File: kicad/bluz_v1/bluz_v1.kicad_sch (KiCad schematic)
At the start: 71 parts, among them J1 USB_B_Micro, J10 Conn, J11 Conn, J12 BTAnt, J2 Conn, J3 Conn, J4 Conn, J5 Conn, J6 Conn, J7 Conn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

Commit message: изменено:      kicad/bluz_v1/bluz_v1.kicad_pcb 	изменено:      kicad/bluz_v1/bluz_v1.kicad_sch
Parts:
- L2: value 47uH -> 47uH LQH31CN470K03L
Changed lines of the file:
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@@
       (effects (font (size 1.27 1.27)) hide)
     )
-    (property "Value" "47uH" (id 1) (at 164.465 28.1741 90))
+    (property "Value" "47uH LQH31CN470K03L" (id 1) (at 159.385 27.305 90))
     (property "Footprint" "Inductor_SMD:L_1206_3216Metric" (id 2) (at 164.465 29.845 0)
       (effects (font (size 1.27 1.27)) hide)
@@
       (effects (font (size 1.27 1.27)) hide)
     )
-    (property "Value" "+BATT" (id 1) (at 151.765 27.94 90)
+    (property "Value" "+BATT" (id 1) (at 147.955 29.845 90)
       (effects (font (size 1.27 1.27)) (justify right))
     )
@@
     )
     (path "/77373934-a013-4003-ae17-82edd2463c24"
-      (reference "L2") (unit 1) (value "47uH") (footprint "Inductor_SMD:L_1206_3216Metric")
+      (reference "L2") (unit 1) (value "47uH LQH31CN470K03L") (footprint "Inductor_SMD:L_1206_3216Metric")
     )
     (path "/fd18f754-2e4f-4eb7-a1de-4025462c7606"

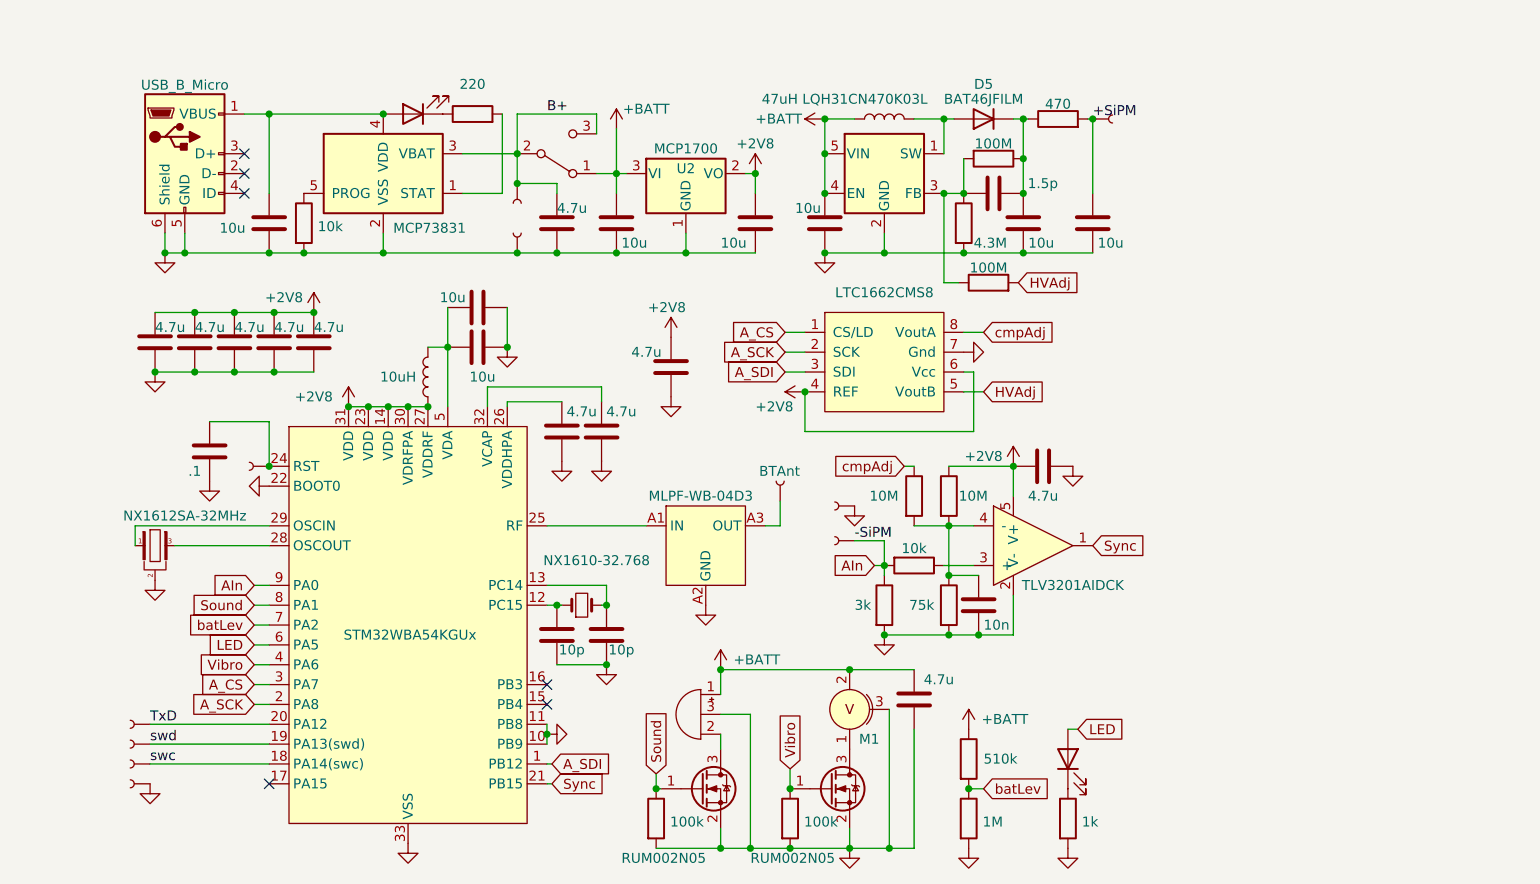
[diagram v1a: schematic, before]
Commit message: изменено:      kicad/bluz_v1/bluz_v1.kicad_sch 	изменено:      stm32cubeide/BluZ_v1/.mxproject 	изменено:      stm32cubeide/BluZ_v1/BluZ_v1.ioc 	изменено:      stm32cubeide/BluZ_v1/Core/Inc/app_conf.h 	изменено:      stm32cubeide/BluZ_v1/Core/Src/main.c 	изменено:      stm32cubeide/BluZ_v1/Release/BluZ_v1.hex 	изменено:      stm32cubeide/BluZ_v1/Release/BluZ_v1.list 	изменено:      stm32cubeide/BluZ_v1/Release/BluZ_v1.map 	изменено:      stm32cubeide/BluZ_v1/Release/makefile
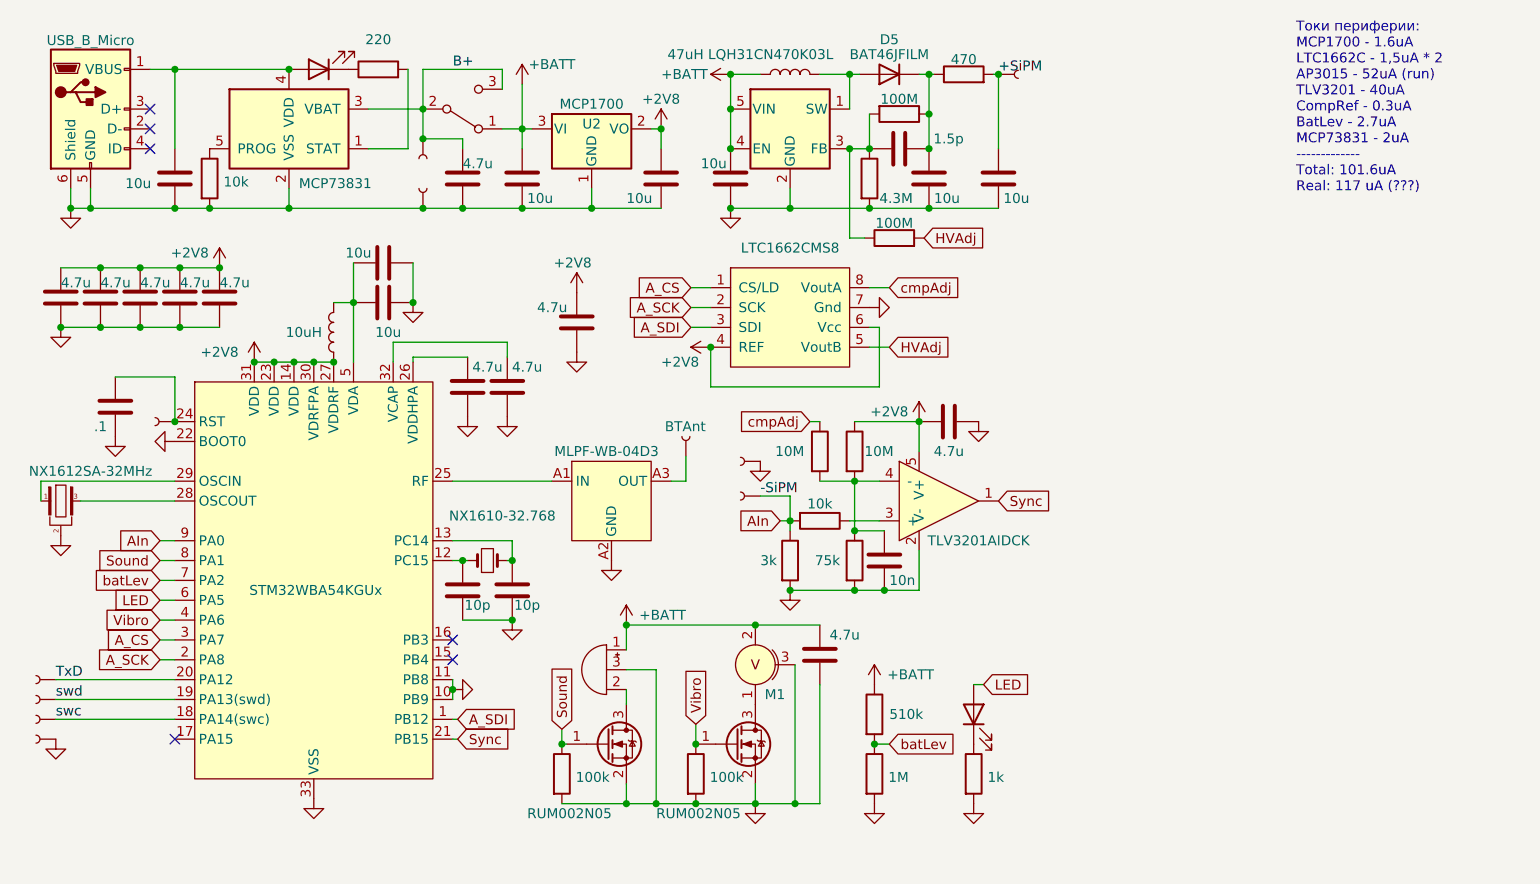
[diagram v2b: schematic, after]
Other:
- note added: "Токи периферии: MCP1700 - 1.6uA LTC1662C - 1,5uA * 2 AP3015 - 52uA (run) TLV3201 - 40uA CompRef - 0.3uA BatLev - 2.7uA MCP73831 - 2uA ------------- Total: 101.6uA Real: 117 uA (???)"
- moved on the sheet: D5, M1, U2

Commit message: изменено:      kicad/bluz_v1/bluz_v1.kicad_pcb 	изменено:      kicad/bluz_v1/bluz_v1.kicad_sch
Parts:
- C16, C19: value 10u -> 22u C3216X5R1V226MTJ00E
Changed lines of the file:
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@@
       (effects (font (size 1.27 1.27)) (justify right) hide)
     )
-    (property "Value" "10u" (id 1) (at 179.705 40.005 0)
+    (property "Value" "22u C3216X5R1V226MTJ00E" (id 1) (at 180.34 40.005 0)
       (effects (font (size 1.27 1.27)) (justify right))
     )
@@
       (effects (font (size 1.27 1.27)) (justify right) hide)
     )
-    (property "Value" "10u" (id 1) (at 170.815 40.005 0)
+    (property "Value" "22u C3216X5R1V226MTJ00E" (id 1) (at 180.34 41.91 0)
       (effects (font (size 1.27 1.27)) (justify right))
     )
@@
     )
     (path "/16bbbb75-6154-486b-84f6-0c1483bc5f51"
-      (reference "C16") (unit 1) (value "10u") (footprint "Capacitor_SMD:C_1206_3216Metric")
+      (reference "C16") (unit 1) (value "22u C3216X5R1V226MTJ00E") (footprint "Capacitor_SMD:C_1206_3216Metric")
     )
     (path "/980a06c5-1cd4-4fc4-8a8a-5c3f1f1b59b0"
@@
     )
     (path "/134867a7-9699-4483-af4a-0e90ac8f8405"
-      (reference "C19") (unit 1) (value "10u") (footprint "Capacitor_SMD:C_1206_3216Metric")
+      (reference "C19") (unit 1) (value "22u C3216X5R1V226MTJ00E") (footprint "Capacitor_SMD:C_1206_3216Metric")
     )
     (path "/6916de32-6e66-4bee-aa98-6c0b14bb45bd"

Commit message: изменено:      kicad/bluz_v1/bluz_v1.kicad_pcb 	изменено:      kicad/bluz_v1/bluz_v1.kicad_prl 	изменено:      kicad/bluz_v1/bluz_v1.kicad_sch 	изменено:      kicad/bluz_v1/fp-info-cache 	изменено:      stm32cubeide/BluZ_v1/.cproject 	изменено:      stm32cubeide/BluZ_v1/.settings/language.settings.xml 	изменено:      stm32cubeide/BluZ_v1/Core/Src/rw_FLASH.c 	изменено:      stm32cubeide/BluZ_v1/Debug/BluZ_v1.elf 	изменено:      stm32cubeide/BluZ_v1/Debug/BluZ_v1.hex 	изменено:      stm32cubeide/BluZ_v1/Debug/BluZ_v1.list 	изменено:      stm32cubeide/BluZ_v1/Debug/BluZ_v1.map 	изменено:      stm32cubeide/BluZ_v1/Debug/Core/Src/app_entry.d 	изменено:      stm32cubeide/BluZ_v1/Debug/Core/Src/app_entry.o 	изменено:      stm32cubeide/BluZ_v1/Debug/Core/Src/main.cyclo 	изменено:      stm32cubeide/BluZ_v1/Debug/Core/Src/main.d 	изменено:      stm32cubeide/BluZ_v1/Debug/Core/Src/main.o 	изменено:      stm32cubeide/BluZ_v1/Debug/Core/Src/main.su 	изменено:      stm32cubeide/BluZ_v1/Debug/Core/Src/stm32wbaxx_hal_msp.cyclo 	изменено:      stm32cubeide/BluZ_v1/Debug/Core/Src/stm32wbaxx_hal_msp.d 	изменено:      stm32cubeide/BluZ_v1/Debug/Core/Src/stm32wbaxx_hal_msp.o 	изменено:      stm32cubeide/BluZ_v1/Debug/Core/Src/stm32wbaxx_hal_msp.su 	изменено:      stm32cubeide/BluZ_v1/Debug/Core/Src/stm32wbaxx_it.cyclo 	изменено:      stm32cubeide/BluZ_v1/Debug/Core/Src/stm32wbaxx_it.d 	изменено:      stm32cubeide/BluZ_v1/Debug/Core/Src/stm32wbaxx_it.o 	изменено:      stm32cubeide/BluZ_v1/Debug/Core/Src/stm32wbaxx_it.su 	изменено:      stm32cubeide/BluZ_v1/Debug/Core/Src/subdir.mk 	изменено:      stm32cubeide/BluZ_v1/Debug/Core/Src/syscalls.o 	изменено:      stm32cubeide/BluZ_v1/Debug/Core/Src/sysmem.o 	изменено:      stm32cubeide/BluZ_v1/Debug/Core/Src/system_stm32wbaxx.o 	изменено:      stm32cubeide/BluZ_v1/Debug/Core/Startup/startup_stm32wba54kgux.o 	изменено:      stm32cubeide/BluZ_v1/Debug/Drivers/STM32WBAxx_HAL_Driver/Src/stm32wbaxx_hal.o 	изменено:      stm32cubeide/BluZ_v1/Debug/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
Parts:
- L2: footprint Inductor_SMD:L_1206_3216Metric -> Inductor_SMD:L_1206_3216Metric_Pad1.42x1.75mm_HandSolder
- R14: value 470 -> 1k
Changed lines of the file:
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@@
     )
     (property "Value" "47uH LQH31CN470K03L" (id 1) (at 147.32 21.59 90))
-    (property "Footprint" "Inductor_SMD:L_1206_3216Metric" (id 2) (at 152.4 24.13 0)
+    (property "Footprint" "Inductor_SMD:L_1206_3216Metric_Pad1.42x1.75mm_HandSolder" (id 2) (at 152.4 24.13 0)
       (effects (font (size 1.27 1.27)) hide)
     )
@@
       (effects (font (size 1.27 1.27)) (justify left) hide)
     )
-    (property "Value" "470" (id 1) (at 174.625 22.225 90))
+    (property "Value" "1k" (id 1) (at 174.625 22.225 90))
     (property "Footprint" "Resistor_SMD:R_0402_1005Metric" (id 2) (at 174.625 25.908 90)
       (effects (font (size 1.27 1.27)) hide)
@@
     )
     (path "/77373934-a013-4003-ae17-82edd2463c24"
-      (reference "L2") (unit 1) (value "47uH LQH31CN470K03L") (footprint "Inductor_SMD:L_1206_3216Metric")
+      (reference "L2") (unit 1) (value "47uH LQH31CN470K03L") (footprint "Inductor_SMD:L_1206_3216Metric_Pad1.42x1.75mm_HandSolder")
     )
     (path "/fd18f754-2e4f-4eb7-a1de-4025462c7606"
@@
     )
     (path "/adf52942-5a78-4ce6-9f92-ba8f0b0fdf88"
-      (reference "R14") (unit 1) (value "470") (footprint "Resistor_SMD:R_0402_1005Metric")
+      (reference "R14") (unit 1) (value "1k") (footprint "Resistor_SMD:R_0402_1005Metric")
     )
     (path "/c8dd2620-be56-4c2f-bce2-f222bc17d9b2"

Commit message: изменено:      Android/BluZ_v1/.idea/deploymentTargetSelector.xml 	изменено:      Android/BluZ_v1/.idea/other.xml 	изменено:      Documents/BluZ.png 	изменено:      kicad/bluz_v1/bluz_v1.kicad_sch
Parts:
- L2: value 47uH LQH31CN470K03L -> 22uH LQH31CN220K03L
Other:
- note added: "Токи периферии: MCP1700 - 1.6uA LTC1662C - 1,5uA * 2 AP3015 - 52uA (run) TLV3201 - 40uA CompRef - 0.3uA BatLev - 2.7uA MCP73831 - 2uA ------------- Total: 101.6uA Real: 89.9uA"
- note removed: "Токи периферии: MCP1700 - 1.6uA LTC1662C - 1,5uA * 2 AP3015 - 52uA (run) TLV3201 - 40uA CompRef - 0.3uA BatLev - 2.7uA MCP73831 - 2uA ------------- Total: 101.6uA Real: 117 uA (???)"
